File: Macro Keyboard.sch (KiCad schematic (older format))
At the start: 0 parts

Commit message: Added PCA9745B16B. Updated schematic. ERC Passes.
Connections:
- no-connect marks 0 -> 3
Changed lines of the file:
@@
 F2 "REnc_A" O R 2200 3950 50
 F3 "REnc_B" O R 2200 4050 50
-F4 "REnc_LED_R" O R 2200 4500 50
-F5 "REnc_LED_G" O R 2200 4600 50
-F6 "REnc_LED_B" O R 2200 4700 50
+F4 "REnc_LED_R_5V" O R 2200 4500 50
+F5 "REnc_LED_G_5V" O R 2200 4600 50
+F6 "REnc_LED_B_5V" O R 2200 4700 50
 F7 "REnc_SW" O R 2200 4150 50
 $EndSheet
@@
 	2200 4500 2500 4500
 $Sheet
-S 2500 4250 750  550
+S 2500 4250 900  550
 U 61A0B364
 F0 "RGB Driver" 50
 F1 "RGBDrvier.sch" 50
-F2 "DRIVER_LED_R" I L 2500 4500 50
-F3 "DRIVER_LED_G" I L 2500 4600 50
-F4 "DRIVER_LED_B" I L 2500 4700 50
-F5 "DRIVER_LED_RCK" I R 3250 4350 50
+F2 "DRIVER_LED_R_5V" I L 2500 4500 50
+F3 "DRIVER_LED_G_5V" I L 2500 4600 50
+F4 "DRIVER_LED_B_5V" I L 2500 4700 50
+F5 "DRIVER_LED_CS_3V3" I R 3400 4350 50
 $EndSheet
 $Sheet
@@
 	5250 3150 6650 3150
 Wire Wire Line
-	3250 4350 3550 4350
-Wire Wire Line
 	2200 3950 2350 3950
 Wire Wire Line
@@
 Wire Wire Line
 	5250 2850 6650 2850
+Wire Wire Line
+	3400 4350 3550 4350
+Wire Wire Line
+	5250 2250 5350 2250
+Wire Wire Line
+	5250 2350 5350 2350
+Wire Wire Line
+	5250 2450 5350 2450
+NoConn ~ 5350 2450
+NoConn ~ 5350 2350
+NoConn ~ 5350 2250
 $EndSCHEMATC

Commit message: design checkpoint
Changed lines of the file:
@@
 S 1250 3900 950  900
 U 61A047C3
-F0 "Rotary Encoder" 50
+F0 "Rotary Encoder 1" 50
 F1 "RotaryEncoder.sch" 50
 F2 "REnc_A" O R 2200 3950 50
@@
 NoConn ~ 5350 2350
 NoConn ~ 5350 2250
+$Sheet
+S 1250 5050 950  900
+U 61A55BF3
+F0 "Rotary Encoder 2" 50
+F1 "RotaryEncoder.sch" 50
+F2 "REnc_A" O R 2200 5100 50
+F3 "REnc_B" O R 2200 5200 50
+F4 "REnc_LED_R_5V" O R 2200 5650 50
+F5 "REnc_LED_G_5V" O R 2200 5750 50
+F6 "REnc_LED_B_5V" O R 2200 5850 50
+F7 "REnc_SW" O R 2200 5300 50
+$EndSheet
 $EndSCHEMATC

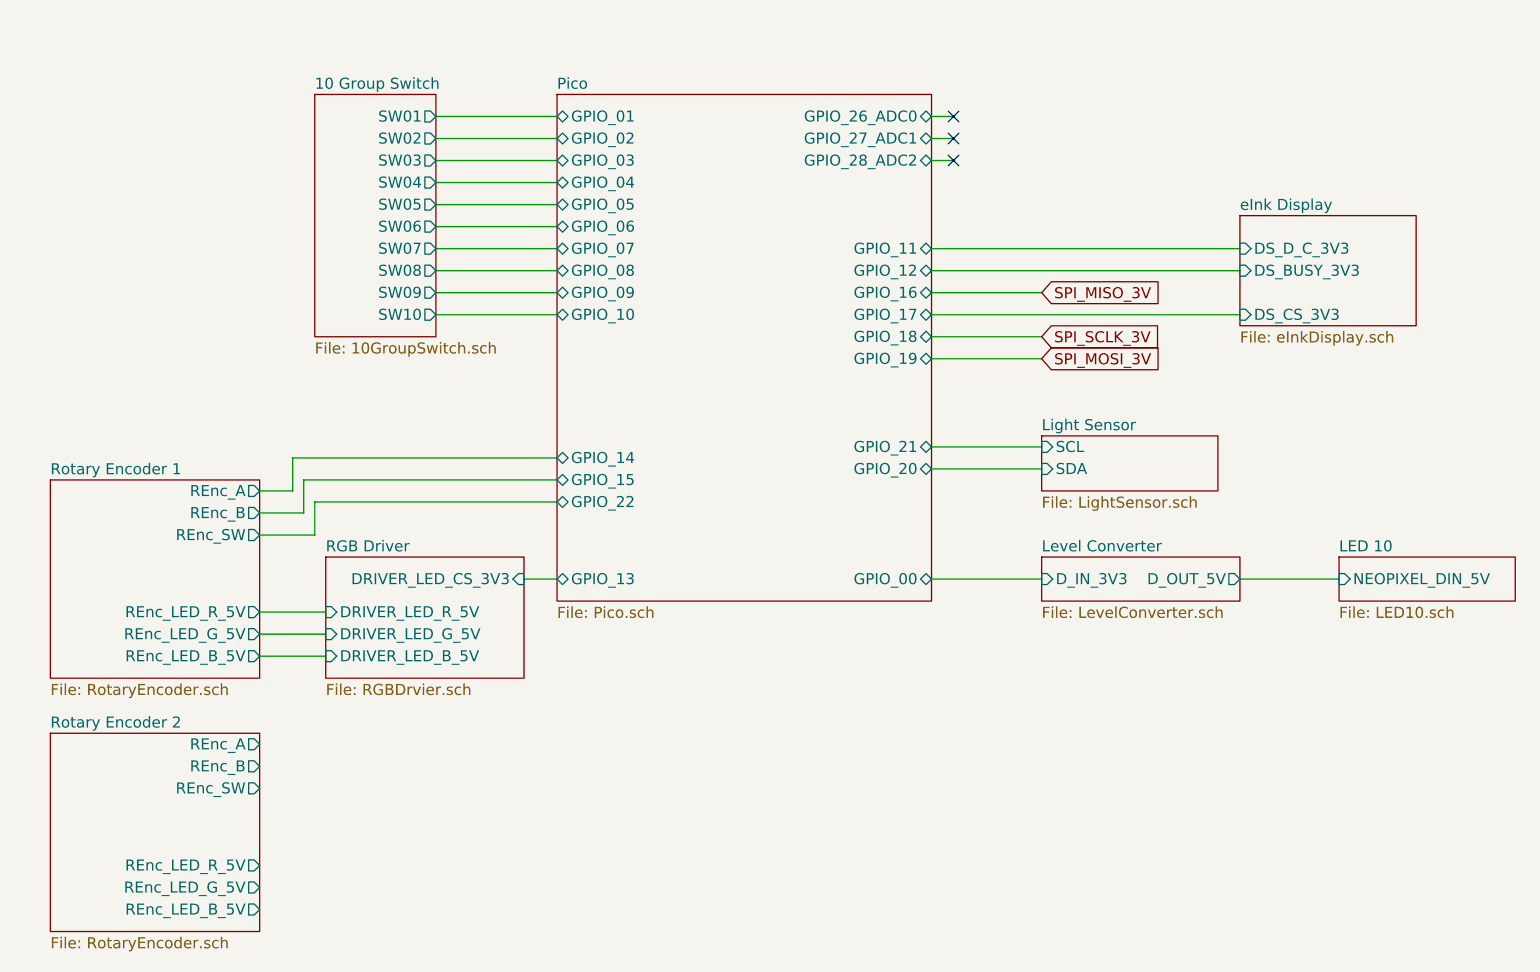
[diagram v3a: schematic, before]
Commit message: Layout completed. Design check passes.
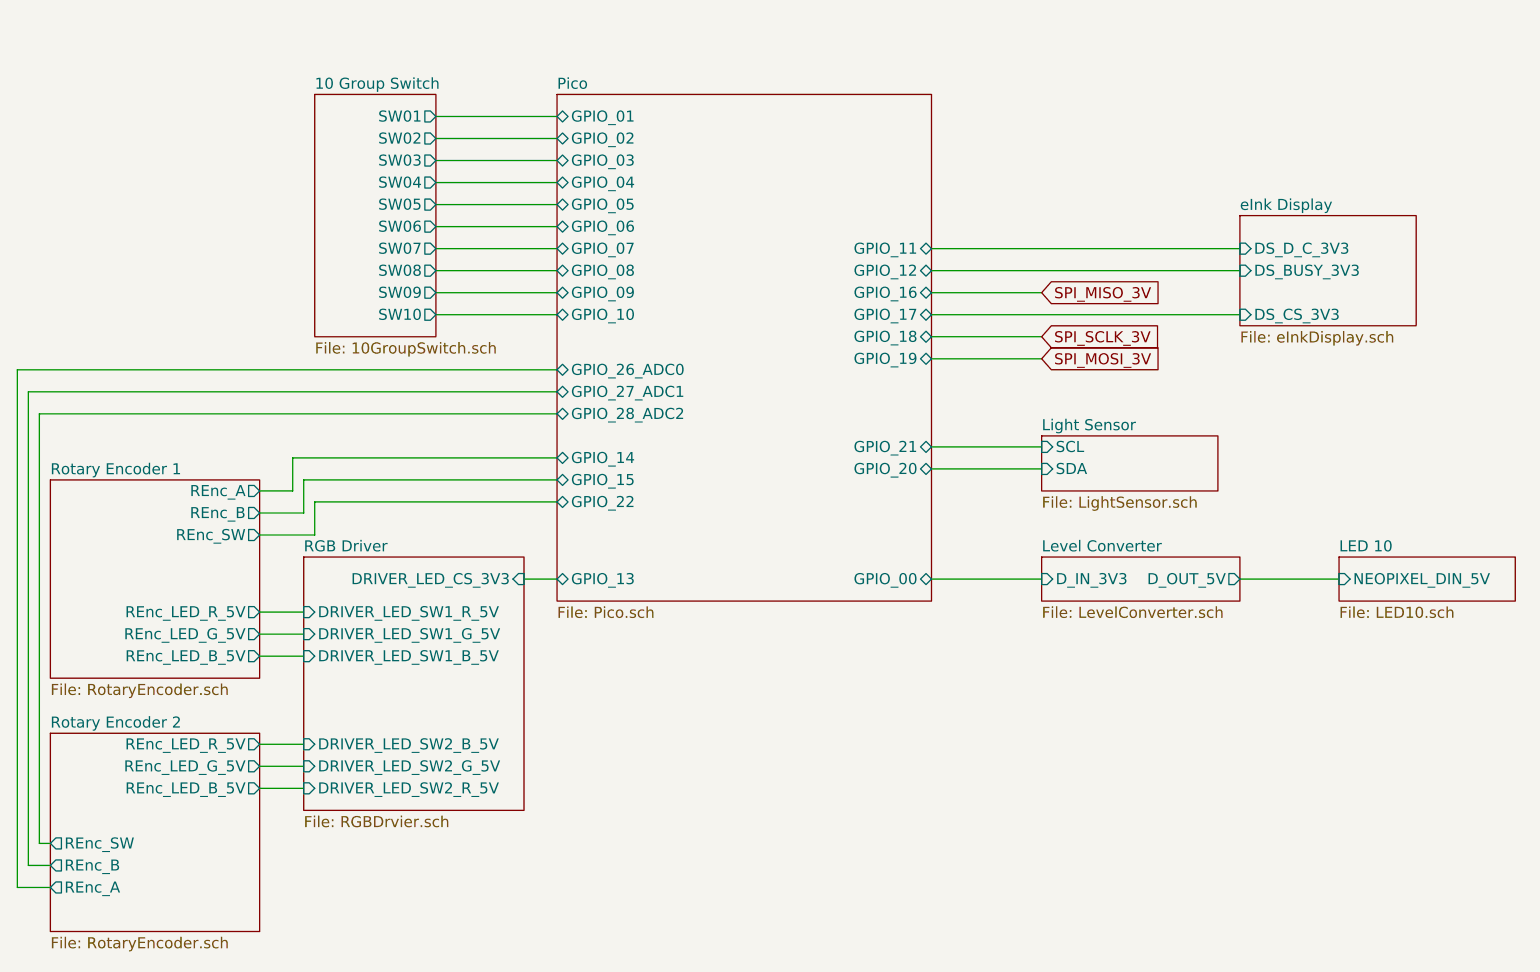
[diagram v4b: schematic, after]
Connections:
- no-connect marks 3 -> 0
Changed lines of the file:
@@
 $EndDescr
-$Sheet
-S 1250 3900 950  900
-U 61A047C3
-F0 "Rotary Encoder 1" 50
-F1 "RotaryEncoder.sch" 50
-F2 "REnc_A" O R 2200 3950 50
-F3 "REnc_B" O R 2200 4050 50
-F4 "REnc_LED_R_5V" O R 2200 4500 50
-F5 "REnc_LED_G_5V" O R 2200 4600 50
-F6 "REnc_LED_B_5V" O R 2200 4700 50
-F7 "REnc_SW" O R 2200 4150 50
-$EndSheet
 $Sheet
 S 5750 3700 800  250
@@
 F2 "NEOPIXEL_DIN_5V" I L 7100 4350 50
 $EndSheet
-Wire Wire Line
-	2500 4700 2200 4700
-Wire Wire Line
-	2200 4600 2500 4600
-Wire Wire Line
-	2200 4500 2500 4500
-$Sheet
-S 2500 4250 900  550
+$Sheet
+S 2400 4250 1000 1150
 U 61A0B364
 F0 "RGB Driver" 50
 F1 "RGBDrvier.sch" 50
-F2 "DRIVER_LED_R_5V" I L 2500 4500 50
-F3 "DRIVER_LED_G_5V" I L 2500 4600 50
-F4 "DRIVER_LED_B_5V" I L 2500 4700 50
-F5 "DRIVER_LED_CS_3V3" I R 3400 4350 50
-$EndSheet
+F2 "DRIVER_LED_CS_3V3" I R 3400 4350 50
+F3 "DRIVER_LED_SW1_R_5V" I L 2400 4500 50
+F4 "DRIVER_LED_SW1_G_5V" I L 2400 4600 50
+F5 "DRIVER_LED_SW1_B_5V" I L 2400 4700 50
+F6 "DRIVER_LED_SW2_B_5V" I L 2400 5100 50
+F7 "DRIVER_LED_SW2_G_5V" I L 2400 5200 50
+F8 "DRIVER_LED_SW2_R_5V" I L 2400 5300 50
+$EndSheet
+Wire Wire Line
+	3550 2250 3000 2250
+Wire Wire Line
+	3000 2350 3550 2350
+Wire Wire Line
+	3550 2450 3000 2450
+Wire Wire Line
+	3000 2550 3550 2550
+Wire Wire Line
+	3550 2650 3000 2650
+Wire Wire Line
+	3000 2750 3550 2750
+Wire Wire Line
+	3550 2850 3000 2850
+Wire Wire Line
+	3000 2950 3550 2950
+Wire Wire Line
+	3550 3050 3000 3050
+Wire Wire Line
+	3000 3150 3550 3150
+$Sheet
+S 6650 2700 800  500
+U 61A7FF0F
+F0 "eInk Display" 50
+F1 "eInkDisplay.sch" 50
+F2 "DS_CS_3V3" I L 6650 3150 50
+F3 "DS_D_C_3V3" I L 6650 2850 50
+F4 "DS_BUSY_3V3" I L 6650 2950 50
+$EndSheet
+Wire Wire Line
+	6650 4350 7100 4350
+Wire Wire Line
+	5250 4350 5750 4350
+Text GLabel 5750 3350 2    50   Input ~ 0
+SPI_MOSI_3V
+Text GLabel 5750 3250 2    50   Input ~ 0
+SPI_SCLK_3V
+Wire Wire Line
+	5250 3050 5750 3050
+Wire Wire Line
+	5250 3250 5750 3250
+Wire Wire Line
+	5250 3350 5750 3350
+Text GLabel 5750 3050 2    50   Input ~ 0
+SPI_MISO_3V
+Wire Wire Line
+	5250 3150 6650 3150
+Wire Wire Line
+	2200 3950 2350 3950
+Wire Wire Line
+	2350 3950 2350 3800
+Wire Wire Line
+	2350 3800 3550 3800
+Wire Wire Line
+	2200 4050 2400 4050
+Wire Wire Line
+	2400 4050 2400 3900
+Wire Wire Line
+	2400 3900 3550 3900
+Wire Wire Line
+	2200 4150 2450 4150
+Wire Wire Line
+	2450 4150 2450 4000
+Wire Wire Line
+	2450 4000 3550 4000
+Wire Wire Line
+	5250 3750 5750 3750
+Wire Wire Line
+	5250 3850 5750 3850
+Wire Wire Line
+	5250 2950 6650 2950
+Wire Wire Line
+	5250 2850 6650 2850
+Wire Wire Line
+	3400 4350 3550 4350
+$Sheet
+S 1250 5050 950  900
+U 61A55BF3
+F0 "Rotary Encoder 2" 50
+F1 "RotaryEncoder.sch" 50
+F2 "REnc_A" O L 1250 5750 50
+F3 "REnc_B" O L 1250 5650 50
+F4 "REnc_LED_R_5V" O R 2200 5100 50
+F5 "REnc_LED_G_5V" O R 2200 5200 50
+F6 "REnc_LED_B_5V" O R 2200 5300 50
+F7 "REnc_SW" O L 1250 5550 50
+$EndSheet
+$Sheet
+S 1250 3900 950  900
+U 61A047C3
+F0 "Rotary Encoder 1" 50
+F1 "RotaryEncoder.sch" 50
+F2 "REnc_A" O R 2200 3950 50
+F3 "REnc_B" O R 2200 4050 50
+F4 "REnc_LED_R_5V" O R 2200 4500 50
+F5 "REnc_LED_G_5V" O R 2200 4600 50
+F6 "REnc_LED_B_5V" O R 2200 4700 50
+F7 "REnc_SW" O R 2200 4150 50
+$EndSheet
+Wire Wire Line
+	2200 4500 2400 4500
+Wire Wire Line
+	2400 4600 2200 4600
+Wire Wire Line
+	2200 4700 2400 4700
+Wire Wire Line
+	2200 5300 2400 5300
+Wire Wire Line
+	2400 5200 2200 5200
+Wire Wire Line
+	2200 5100 2400 5100
 $Sheet
 S 3550 2150 1700 2300
@@
 F23 "GPIO_21" B R 5250 3750 50
 F24 "GPIO_22" B L 3550 4000 50
-F25 "GPIO_26_ADC0" B R 5250 2250 50
-F26 "GPIO_27_ADC1" B R 5250 2350 50
-F27 "GPIO_28_ADC2" B R 5250 2450 50
-$EndSheet
-Wire Wire Line
-	3550 2250 3000 2250
-Wire Wire Line
-	3000 2350 3550 2350
-Wire Wire Line
-	3550 2450 3000 2450
-Wire Wire Line
-	3000 2550 3550 2550
-Wire Wire Line
-	3550 2650 3000 2650
-Wire Wire Line
-	3000 2750 3550 2750
-Wire Wire Line
-	3550 2850 3000 2850
-Wire Wire Line
-	3000 2950 3550 2950
-Wire Wire Line
-	3550 3050 3000 3050
-Wire Wire Line
-	3000 3150 3550 3150
-$Sheet
-S 6650 2700 800  500
-U 61A7FF0F
-F0 "eInk Display" 50
-F1 "eInkDisplay.sch" 50
-F2 "DS_CS_3V3" I L 6650 3150 50
-F3 "DS_D_C_3V3" I L 6650 2850 50
-F4 "DS_BUSY_3V3" I L 6650 2950 50
-$EndSheet
-Wire Wire Line
-	6650 4350 7100 4350
-Wire Wire Line
-	5250 4350 5750 4350
-Text GLabel 5750 3350 2    50   Input ~ 0
-SPI_MOSI_3V
-Text GLabel 5750 3250 2    50   Input ~ 0
-SPI_SCLK_3V
-Wire Wire Line
-	5250 3050 5750 3050
-Wire Wire Line
-	5250 3250 5750 3250
-Wire Wire Line
-	5250 3350 5750 3350
-Text GLabel 5750 3050 2    50   Input ~ 0
-SPI_MISO_3V
-Wire Wire Line
-	5250 3150 6650 3150
-Wire Wire Line
-	2200 3950 2350 3950
-Wire Wire Line
-	2350 3950 2350 3800
-Wire Wire Line
-	2350 3800 3550 3800
-Wire Wire Line
-	2200 4050 2400 4050
-Wire Wire Line
-	2400 4050 2400 3900
-Wire Wire Line
-	2400 3900 3550 3900
-Wire Wire Line
-	2200 4150 2450 4150
-Wire Wire Line
-	2450 4150 2450 4000
-Wire Wire Line
-	2450 4000 3550 4000
-Wire Wire Line
-	5250 3750 5750 3750
-Wire Wire Line
-	5250 3850 5750 3850
-Wire Wire Line
-	5250 2950 6650 2950
-Wire Wire Line
-	5250 2850 6650 2850
-Wire Wire Line
-	3400 4350 3550 4350
-Wire Wire Line
-	5250 2250 5350 2250
-Wire Wire Line
-	5250 2350 5350 2350
-Wire Wire Line
-	5250 2450 5350 2450
-NoConn ~ 5350 2450
-NoConn ~ 5350 2350
-NoConn ~ 5350 2250
-$Sheet
-S 1250 5050 950  900
-U 61A55BF3
-F0 "Rotary Encoder 2" 50
-F1 "RotaryEncoder.sch" 50
-F2 "REnc_A" O R 2200 5100 50
-F3 "REnc_B" O R 2200 5200 50
-F4 "REnc_LED_R_5V" O R 2200 5650 50
-F5 "REnc_LED_G_5V" O R 2200 5750 50
-F6 "REnc_LED_B_5V" O R 2200 5850 50
-F7 "REnc_SW" O R 2200 5300 50
-$EndSheet
+F25 "GPIO_26_ADC0" B L 3550 3400 50
+F26 "GPIO_27_ADC1" B L 3550 3500 50
+F27 "GPIO_28_ADC2" B L 3550 3600 50
+$EndSheet
+Wire Wire Line
+	1250 5550 1200 5550
+Wire Wire Line
+	1200 5550 1200 3600
+Wire Wire Line
+	1200 3600 3550 3600
+Wire Wire Line
+	1250 5650 1150 5650
+Wire Wire Line
+	1150 5650 1150 3500
+Wire Wire Line
+	1150 3500 3550 3500
+Wire Wire Line
+	1250 5750 1100 5750
+Wire Wire Line
+	1100 5750 1100 3400
+Wire Wire Line
+	1100 3400 3550 3400
 $EndSCHEMATC

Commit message: Added labels
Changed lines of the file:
@@
 Wire Wire Line
 	1100 3400 3550 3400
+Text Label 5250 2850 0    50   ~ 0
+DS_D_C_3V3
+Text Label 5250 2950 0    50   ~ 0
+DS_BUSY_3V3
+Text Label 5250 3050 0    50   ~ 0
+SPI_MISO_3V
+Text Label 5250 3250 0    50   ~ 0
+SPI_SCLK_3V
+Text Label 5250 3350 0    50   ~ 0
+SPI_MOSI_3V
+Text Label 5250 3150 0    50   ~ 0
+DS_CS_3V3
+Text Label 5250 3750 0    50   ~ 0
+SCL
+Text Label 5250 3850 0    50   ~ 0
+SDA
+Text Label 5250 4350 0    50   ~ 0
+D_IN_3V3
+Text Label 3500 4350 3    50   ~ 0
+DRIVER_LED_CS
+Text Label 2450 3800 0    50   ~ 0
+REnc_1_A
+Text Label 2450 3900 0    50   ~ 0
+REnc_1_B
+Text Label 2450 4000 0    50   ~ 0
+REnc_1_SW
+Text Label 2450 3400 0    50   ~ 0
+REnc_2_A
+Text Label 2450 3500 0    50   ~ 0
+REnc_2_B
+Text Label 2450 3600 0    50   ~ 0
+REnc_2_SW
+Text Label 3150 2250 0    50   ~ 0
+SW1
+Text Label 3150 2350 0    50   ~ 0
+SW2
+Text Label 3150 2450 0    50   ~ 0
+SW3
+Text Label 3150 2550 0    50   ~ 0
+SW4
+Text Label 3150 2650 0    50   ~ 0
+SW5
+Text Label 3150 2750 0    50   ~ 0
+SW6
+Text Label 3150 2850 0    50   ~ 0
+SW7
+Text Label 3150 2950 0    50   ~ 0
+SW8
+Text Label 3150 3050 0    50   ~ 0
+SW9
+Text Label 3150 3150 0    50   ~ 0
+SW10
 $EndSCHEMATC

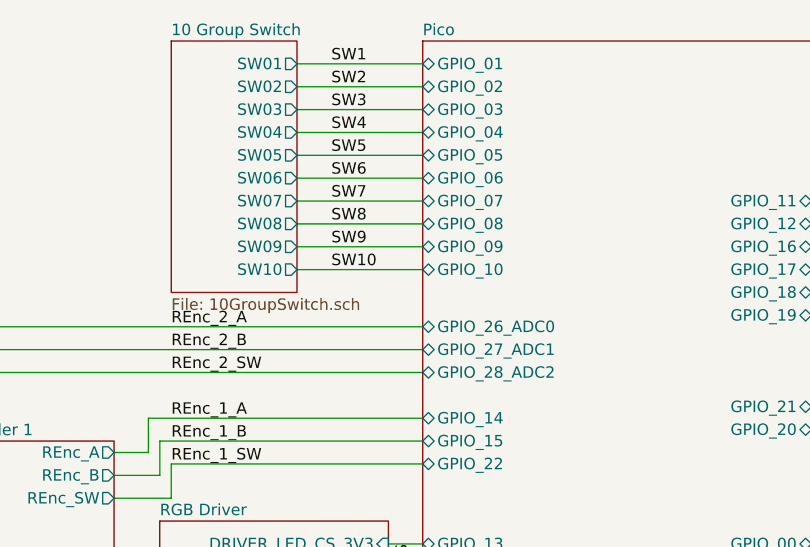
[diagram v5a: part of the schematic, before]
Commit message: Re-arrange pins and cleanup routing
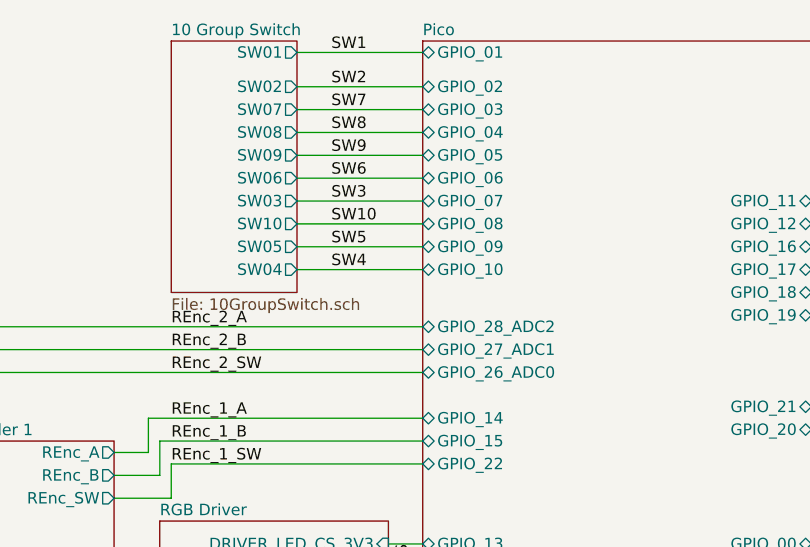
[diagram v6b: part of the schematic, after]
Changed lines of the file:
@@
 F0 "10 Group Switch" 50
 F1 "10GroupSwitch.sch" 50
-F2 "SW01" O R 3000 2250 50
+F2 "SW01" O R 3000 2200 50
 F3 "SW02" O R 3000 2350 50
-F4 "SW03" O R 3000 2450 50
-F5 "SW04" O R 3000 2550 50
-F6 "SW05" O R 3000 2650 50
+F4 "SW03" O R 3000 2850 50
+F5 "SW04" O R 3000 3150 50
+F6 "SW05" O R 3000 3050 50
 F7 "SW06" O R 3000 2750 50
-F8 "SW07" O R 3000 2850 50
-F9 "SW08" O R 3000 2950 50
-F10 "SW09" O R 3000 3050 50
-F11 "SW10" O R 3000 3150 50
+F8 "SW07" O R 3000 2450 50
+F9 "SW08" O R 3000 2550 50
+F10 "SW09" O R 3000 2650 50
+F11 "SW10" O R 3000 2950 50
 $EndSheet
 $Sheet
@@
 $EndSheet
 Wire Wire Line
-	3550 2250 3000 2250
-Wire Wire Line
 	3000 2350 3550 2350
 Wire Wire Line
@@
 Wire Wire Line
 	2200 5100 2400 5100
-$Sheet
-S 3550 2150 1700 2300
-U 61A0B536
-F0 "Pico" 50
-F1 "Pico.sch" 50
-F2 "GPIO_00" B R 5250 4350 50
-F3 "GPIO_01" B L 3550 2250 50
-F4 "GPIO_02" B L 3550 2350 50
-F5 "GPIO_03" B L 3550 2450 50
-F6 "GPIO_04" B L 3550 2550 50
-F7 "GPIO_05" B L 3550 2650 50
-F8 "GPIO_06" B L 3550 2750 50
-F9 "GPIO_07" B L 3550 2850 50
-F10 "GPIO_08" B L 3550 2950 50
-F11 "GPIO_09" B L 3550 3050 50
-F12 "GPIO_10" B L 3550 3150 50
-F13 "GPIO_11" B R 5250 2850 50
-F14 "GPIO_12" B R 5250 2950 50
-F15 "GPIO_13" B L 3550 4350 50
-F16 "GPIO_14" B L 3550 3800 50
-F17 "GPIO_15" B L 3550 3900 50
-F18 "GPIO_16" B R 5250 3050 50
-F19 "GPIO_17" B R 5250 3150 50
-F20 "GPIO_18" B R 5250 3250 50
-F21 "GPIO_19" B R 5250 3350 50
-F22 "GPIO_20" B R 5250 3850 50
-F23 "GPIO_21" B R 5250 3750 50
-F24 "GPIO_22" B L 3550 4000 50
-F25 "GPIO_26_ADC0" B L 3550 3400 50
-F26 "GPIO_27_ADC1" B L 3550 3500 50
-F27 "GPIO_28_ADC2" B L 3550 3600 50
-$EndSheet
 Wire Wire Line
 	1250 5550 1200 5550
@@
 Text Label 2450 3600 0    50   ~ 0
 REnc_2_SW
-Text Label 3150 2250 0    50   ~ 0
+Text Label 3150 2200 0    50   ~ 0
 SW1
 Text Label 3150 2350 0    50   ~ 0
 SW2
-Text Label 3150 2450 0    50   ~ 0
+Text Label 3150 2850 0    50   ~ 0
 SW3
-Text Label 3150 2550 0    50   ~ 0
+Text Label 3150 3150 0    50   ~ 0
 SW4
-Text Label 3150 2650 0    50   ~ 0
+Text Label 3150 3050 0    50   ~ 0
 SW5
 Text Label 3150 2750 0    50   ~ 0
 SW6
-Text Label 3150 2850 0    50   ~ 0
+Text Label 3150 2450 0    50   ~ 0
 SW7
+Text Label 3150 2550 0    50   ~ 0
+SW8
+Text Label 3150 2650 0    50   ~ 0
+SW9
 Text Label 3150 2950 0    50   ~ 0
-SW8
-Text Label 3150 3050 0    50   ~ 0
-SW9
-Text Label 3150 3150 0    50   ~ 0
 SW10
+Wire Wire Line
+	3000 2200 3550 2200
+$Sheet
+S 3550 2150 1700 2300
+U 61A0B536
+F0 "Pico" 50
+F1 "Pico.sch" 50
+F2 "GPIO_00" B R 5250 4350 50
+F3 "GPIO_01" B L 3550 2200 50
+F4 "GPIO_02" B L 3550 2350 50
+F5 "GPIO_03" B L 3550 2450 50
+F6 "GPIO_04" B L 3550 2550 50
+F7 "GPIO_05" B L 3550 2650 50
+F8 "GPIO_06" B L 3550 2750 50
+F9 "GPIO_07" B L 3550 2850 50
+F10 "GPIO_08" B L 3550 2950 50
+F11 "GPIO_09" B L 3550 3050 50
+F12 "GPIO_10" B L 3550 3150 50
+F13 "GPIO_11" B R 5250 2850 50
+F14 "GPIO_12" B R 5250 2950 50
+F15 "GPIO_13" B L 3550 4350 50
+F16 "GPIO_14" B L 3550 3800 50
+F17 "GPIO_15" B L 3550 3900 50
+F18 "GPIO_16" B R 5250 3050 50
+F19 "GPIO_17" B R 5250 3150 50
+F20 "GPIO_18" B R 5250 3250 50
+F21 "GPIO_19" B R 5250 3350 50
+F22 "GPIO_20" B R 5250 3850 50
+F23 "GPIO_21" B R 5250 3750 50
+F24 "GPIO_22" B L 3550 4000 50
+F25 "GPIO_26_ADC0" B L 3550 3600 50
+F26 "GPIO_27_ADC1" B L 3550 3500 50
+F27 "GPIO_28_ADC2" B L 3550 3400 50
+$EndSheet
 $EndSCHEMATC

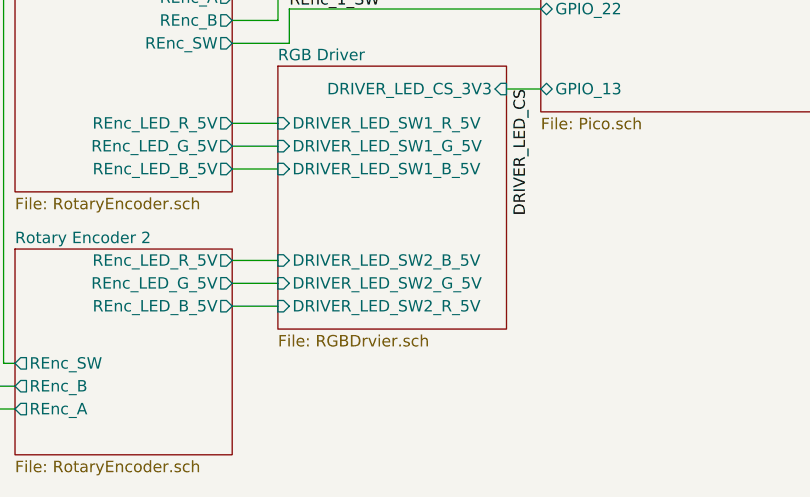
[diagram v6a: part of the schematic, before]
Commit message: Fixed wiring for rotary encoder 2. R and B pins were swapped.
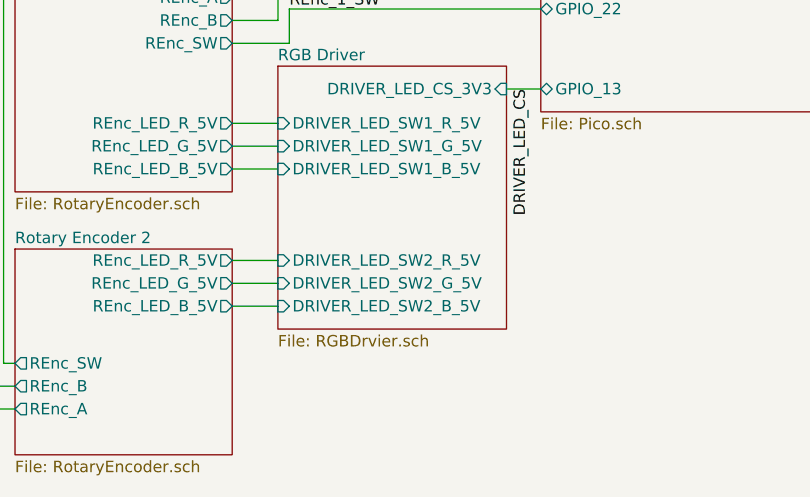
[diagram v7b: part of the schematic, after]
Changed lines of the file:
@@
 F4 "DRIVER_LED_SW1_G_5V" I L 2400 4600 50
 F5 "DRIVER_LED_SW1_B_5V" I L 2400 4700 50
-F6 "DRIVER_LED_SW2_B_5V" I L 2400 5100 50
+F6 "DRIVER_LED_SW2_B_5V" I L 2400 5300 50
 F7 "DRIVER_LED_SW2_G_5V" I L 2400 5200 50
-F8 "DRIVER_LED_SW2_R_5V" I L 2400 5300 50
+F8 "DRIVER_LED_SW2_R_5V" I L 2400 5100 50
 $EndSheet
 Wire Wire Line
